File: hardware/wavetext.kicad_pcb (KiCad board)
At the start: 2 copper layers, 150 x 30 mm, 31 parts, among them IC0 ATTINY2313A-S, P1 CONN_6, P2 CONN_1, P3 CONN_1, Q1 OPTO_NPN, SW0 DUAL_SWITCH_INV, SW1 SW_PUSH, U0 ST L78L33ACUTR

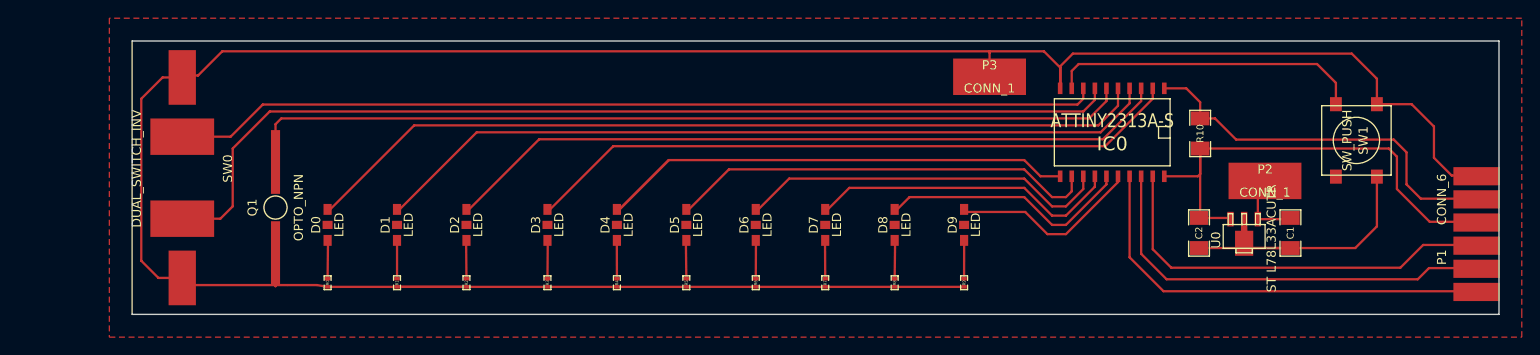
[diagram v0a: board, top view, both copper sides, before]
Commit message: PCB final, breitere Leiterbahnen, spannungsregler richtigrum
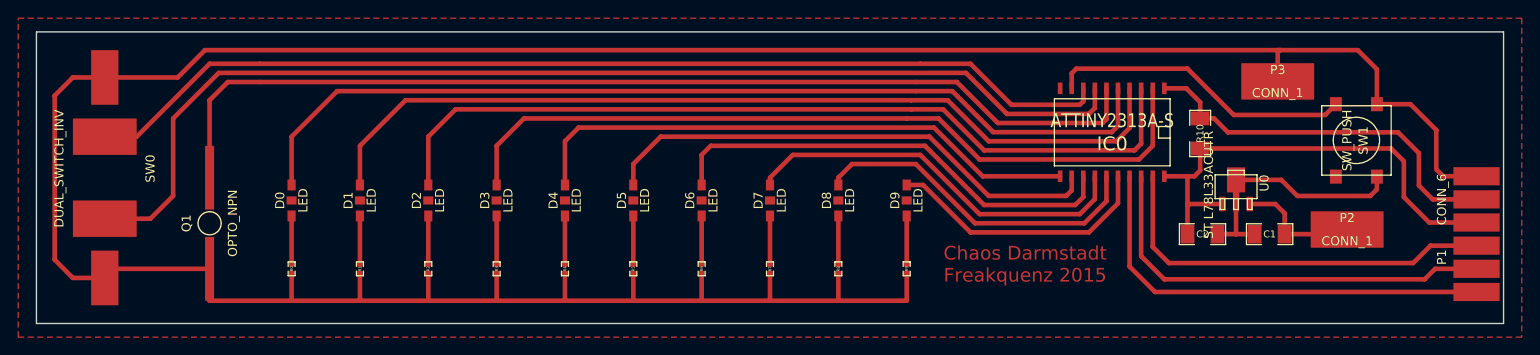
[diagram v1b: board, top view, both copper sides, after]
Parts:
- moved P3 31.6 mm to (275.7, 154.4)
- moved P2 10.5 mm to (283.3, 170.7)
- moved SW0 8.50 mm to (147.0, 176.0)
- moved Q1 7.44 mm to (158.5, 170.0)
- moved D9 6.85 mm to (235.0, 167.5)
- moved D8 6.74 mm to (227.5, 167.5)
- moved D7 6.63 mm to (220.0, 167.5)
- moved D6 6.52 mm to (212.5, 167.5)
- moved R9 6.48 mm to (235.0, 175.0)
- moved D5 6.41 mm to (205.0, 167.5)
- moved R8 6.37 mm to (227.5, 175.0)
- moved D4 6.30 mm to (197.5, 167.5)
- moved R7 6.25 mm to (220.0, 175.0)
- moved D3 6.19 mm to (190.0, 167.5)
- moved R6 6.13 mm to (212.5, 175.0)
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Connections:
- C2 pad 1: N-0000013 (its old number) -> N-0000018
- IC0 pad 20: N-0000013 (its old number) -> N-0000018
- P1 pad 4: N-0000013 (its old number) -> N-0000018
- R10 pad 1: N-0000013 (its old number) -> N-0000018
- U0 pad 1: VCC -> N-0000018
- U0 pad 3: N-0000013 (its old number) -> VCC
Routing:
- net N-0000013 (its old number): track 53.7 -> 0.00 mm
- net N-0000018: track 0.00 -> 53.1 mm
- net GND: track 325.7 -> 344.8 mm
- net N-0000010: track 97.8 -> 113.2 mm
- net N-0000015: track 110.5 -> 124.5 mm
- net N-000007: track 72.7 -> 86.3 mm
- net N-000001: track 80.5 -> 93.0 mm
- net N-0000016: track 101.7 -> 114.1 mm
- net N-000009: track 93.5 -> 104.3 mm
- net N-000008: track 87.0 -> 97.6 mm
- net N-000004: track 40.9 -> 50.9 mm
- net N-000002: track 27.9 -> 37.3 mm
- net N-000003: track 34.4 -> 43.4 mm
- net N-000005: track 47.4 -> 56.1 mm
- net N-0000012: track 20.9 -> 29.6 mm
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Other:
- board size 150 x 30 mm -> 161 x 32 mm
- net class dick added: clearance 0.254, trace_width 0.508, via_dia 0.889, via_drill 0.635
- board text added: "Chaos Darmstadt Freakquenz 2015"
